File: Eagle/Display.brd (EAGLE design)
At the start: 100 x 33 mm, 79 parts, among them Q0A 310mA/60V/1.6Ω, Q0B 310mA/60V/1.6Ω, Q0C 310mA/60V/1.6Ω, Q10 310mA/60V/1.6Ω, Q11 310mA/60V/1.6Ω, Q12 310mA/60V/1.6Ω, Q13 310mA/60V/1.6Ω, Q14 310mA/60V/1.6Ω, Q15 310mA/60V/1.6Ω, Q16 310mA/60V/1.6Ω, Q17 310mA/60V/1.6Ω, Q18 310mA/60V/1.6Ω, Q19 310mA/60V/1.6Ω, Q1A 310mA/60V/1.6Ω, Q1B 310mA/60V/1.6Ω, Q1C 310mA/60V/1.6Ω, Q20 310mA/60V/1.6Ω, Q21 310mA/60V/1.6Ω, Q22A 310mA/60V/1.6Ω, Q22B 310mA/60V/1.6Ω, Q22C 310mA/60V/1.6Ω, Q22D 310mA/60V/1.6Ω, Q23 310mA/60V/1.6Ω, Q24 310mA/60V/1.6Ω, Q25 310mA/60V/1.6Ω, Q26 310mA/60V/1.6Ω, Q2A 310mA/60V/1.6Ω, Q2B 310mA/60V/1.6Ω, Q2C 310mA/60V/1.6Ω, Q3A 310mA/60V/1.6Ω, Q3B 310mA/60V/1.6Ω, Q3C 310mA/60V/1.6Ω, Q4A 310mA/60V/1.6Ω, Q4B 310mA/60V/1.6Ω, Q4C 310mA/60V/1.6Ω, Q5A 310mA/60V/1.6Ω, Q5B 310mA/60V/1.6Ω, Q5C 310mA/60V/1.6Ω, Q6A 310mA/60V/1.6Ω, Q6B 310mA/60V/1.6Ω, Q6C 310mA/60V/1.6Ω, Q7A 310mA/60V/1.6Ω, Q7B 310mA/60V/1.6Ω, Q7C 310mA/60V/1.6Ω, Q8A 310mA/60V/1.6Ω, Q8B 310mA/60V/1.6Ω, Q8C 310mA/60V/1.6Ω, Q9A 310mA/60V/1.6Ω, Q9B 310mA/60V/1.6Ω

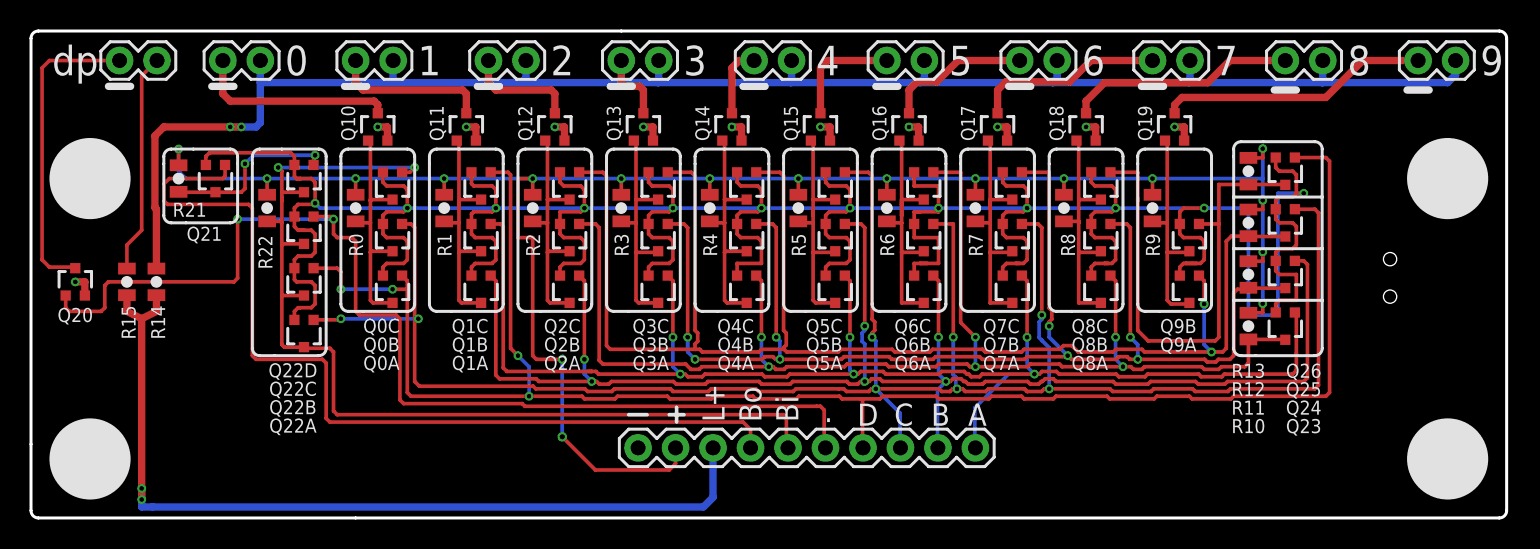
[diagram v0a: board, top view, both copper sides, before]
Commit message: Rerouted for SOT23
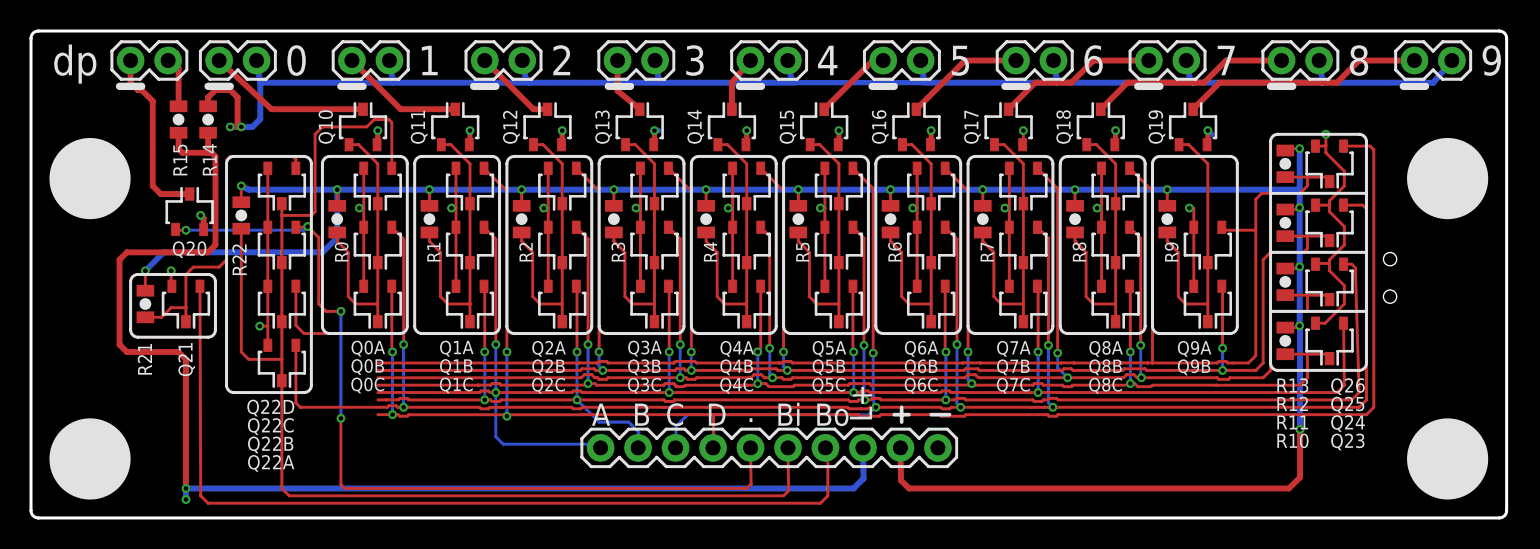
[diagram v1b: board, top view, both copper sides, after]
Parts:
- Q0A, Q0B, Q0C, Q10, Q11, Q12, Q13, Q14, Q15, Q16, Q17, Q18, Q19, Q1A, Q1B, Q1C, Q20, Q21, Q22A, Q22B, Q22C, Q22D, Q23, Q24, Q25, Q26, Q2A, Q2B, Q2C, Q3A, Q3B, Q3C, Q4A, Q4B, Q4C, Q5A, Q5B, Q5C, Q6A, Q6B, Q6C, Q7A, Q7B, Q7C, Q8A, Q8B, Q8C, Q9A, Q9B: device SparkFun-DiscreteSemi:SOT323 -> XSNOR:SOT23
- R0, R1, R10, R11, R12, R13, R14, R15, R2, R21, R22, R3, R4, R5, R6, R7, R8, R9: device SparkFun-Resistors:0805 -> XSNOR:0805
- moved J11 25.4 mm to (38.6, 4.75), turned to 0 degrees
- moved R14 11.5 mm to (12.0, 27.0)
- moved R15 11.5 mm to (10.0, 27.0)
- moved Q20 9.09 mm to (10.8, 20.8)
- moved R21 8.79 mm to (7.75, 14.5)
- moved Q21 8.73 mm to (10.5, 14.5)
- moved Q23 3.16 mm to (88.0, 12.0)
- moved Q24 3.04 mm to (88.0, 16.0)
- moved Q26 3.04 mm to (88.0, 24.0)
- moved Q25 3.00 mm to (88.0, 20.0)
- moved R10 2.69 mm to (85.0, 12.0)
- moved R11 2.55 mm to (85.0, 16.0)
- moved R13 2.55 mm to (85.0, 24.0)
- moved Q22A 2.50 mm to (17.0, 10.5)
- moved R12 2.50 mm to (85.0, 20.0)
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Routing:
- net GND: track 268.2 -> 127.8 mm, vias 23 -> 24
- net /D: track 34.9 -> 94.7 mm
- net /B: track 92.2 -> 119.3 mm
- net LEDPWR1: track 60.3 -> 86.5 mm
- net /C: track 101.3 -> 124.2 mm, vias 2 -> 8
- net VCC: track 136.7 -> 158.9 mm, vias 18 -> 17
- net /A: track 88.4 -> 109.3 mm, vias 6 -> 8
- net C: track 142.1 -> 162.0 mm
- net RBO: track 68.9 -> 84.6 mm, vias 2 -> 0
- net A: track 98.7 -> 113.8 mm, vias 6 -> 8
- net DP: track 74.5 -> 59.4 mm, vias 2 -> 4
- net B: track 104.5 -> 118.1 mm, vias 6 -> 8
- net N$12: track 14.9 -> 3.52 mm
- net LEDPWR: track 116.1 -> 106.1 mm
- net /RBI: track 12.3 -> 21.6 mm, vias 2 -> 0
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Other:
- outline, holes or cut-outs redrawn
- board text added: "14"
- board text added: "23"
- board text added: "32"
- board text added: "41"
- board text added: "50"
- board text added: "59"
- board text added: "68"
- board text added: "77"
- board text added: "86"
- board text added: "95"
- board text added: "Display Driver"
- board text added: "SmallRoomLabs"
- board text removed: "Display Driver rev1"

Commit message: Cleanups of PCBs
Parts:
- removed J11: (no value), SparkFun-Connectors:1X10
- added JP1: (no value), XSNOR:1X10/90
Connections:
- net A: now also JP1.1; no longer J11.1
- net B: now also JP1.2; no longer J11.2
- net C: now also JP1.3; no longer J11.3
- net D: now also JP1.4; no longer J11.4
- net DP: now also JP1.5; no longer J11.5
- net GND: now also JP1.10; no longer J11.10
- net LEDPWR1: now also JP1.8; no longer J11.8
- net RBI: now also JP1.7; no longer J11.7
- net RBO: now also JP1.6; no longer J11.6
- net VCC: now also JP1.9; no longer J11.9

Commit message: Silk cleanup. Routing of GND instead of floodfill
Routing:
- net GND: track 127.8 -> 350.9 mm
- net /D: track 94.7 -> 40.4 mm
- net /B: track 119.3 -> 97.3 mm
- net /C: track 124.2 -> 108.1 mm, vias 8 -> 2
- net /A: track 109.3 -> 94.3 mm, vias 8 -> 6
- net A: track 113.8 -> 100.4 mm, vias 8 -> 7
- net B: track 118.1 -> 109.7 mm, vias 8 -> 6
- net LEDPWR1: track 86.5 -> 84.6 mm
- net RBO: track 84.6 -> 82.8 mm
- net D: track 125.7 -> 123.9 mm
- net N$14: track 16.4 -> 17.7 mm
- net N$9: track 5.37 -> 6.71 mm
- net N$6: track 5.62 -> 6.89 mm
- net C: track 162.0 -> 160.8 mm, vias 8 -> 6
- net DP: track 59.4 -> 58.3 mm
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- removed copper zone on layer 16, net GND
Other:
- board text added: "Display driver rev1"
- board text removed: "Display Driver"

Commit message: Minor cleanup of board
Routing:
- net N$15: track 12.5 -> 11.4 mm
